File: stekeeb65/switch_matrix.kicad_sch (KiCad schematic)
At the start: 136 parts

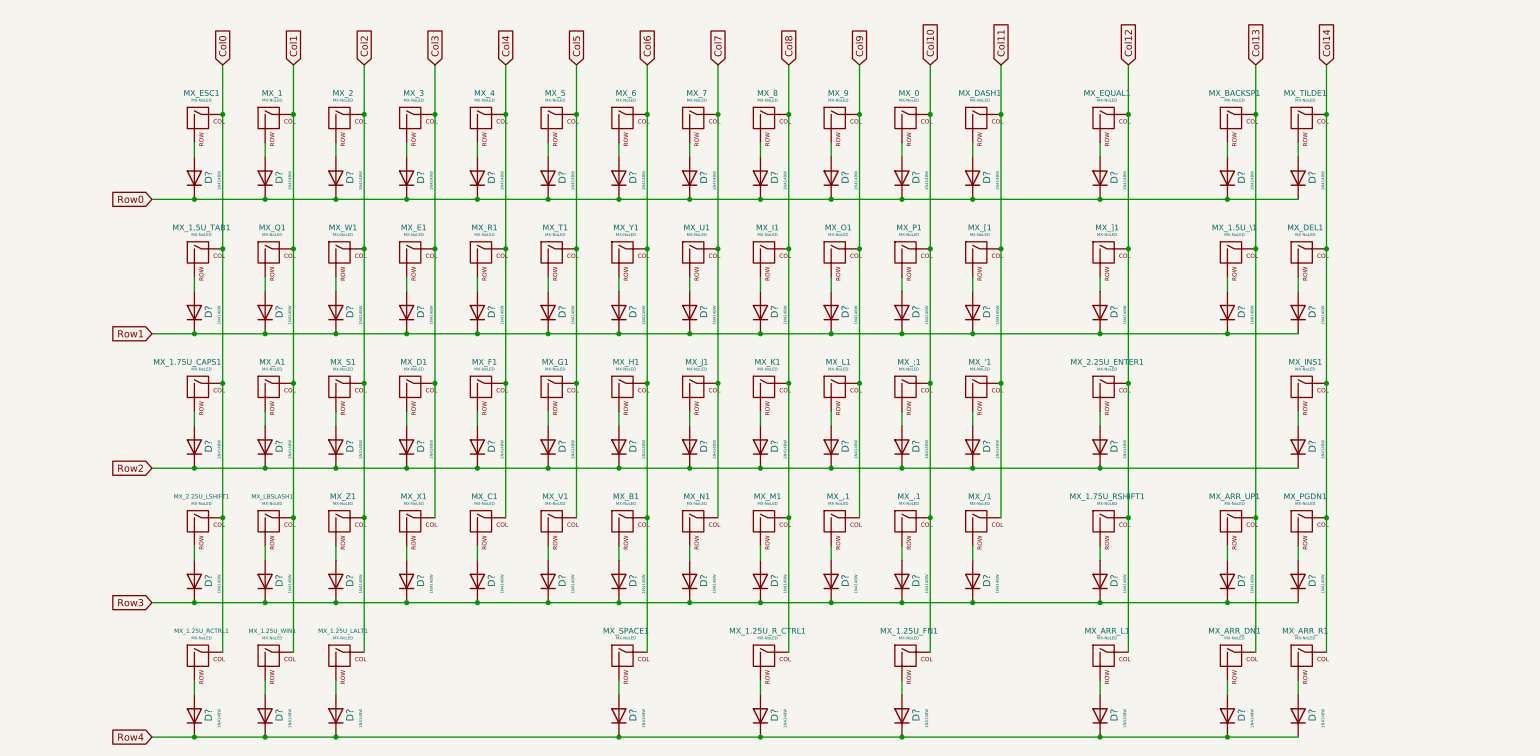
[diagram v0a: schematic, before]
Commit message: Adding keyboard footprints
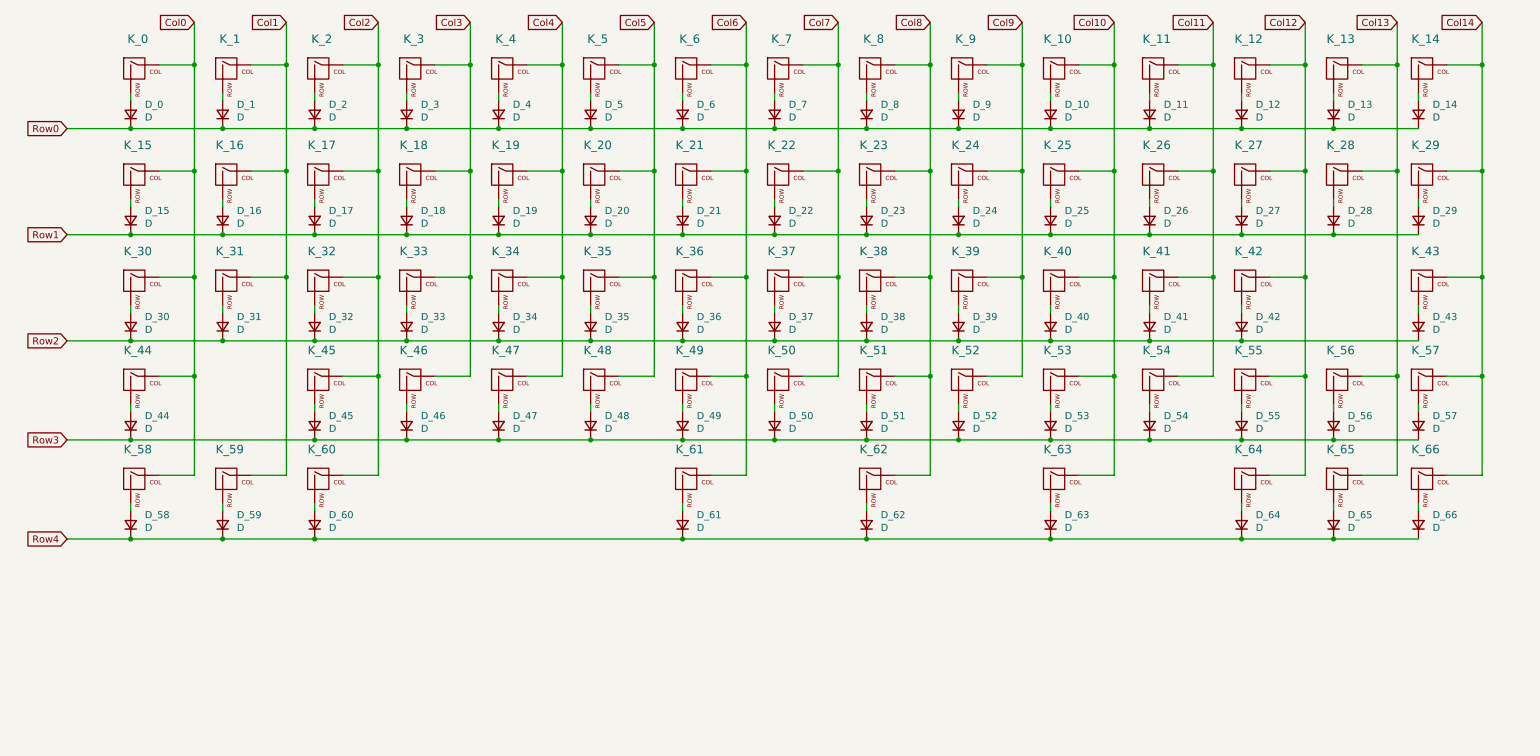
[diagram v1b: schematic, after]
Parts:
- removed D? (x68): 1N4148W, Diode_SMD:D_SOD-123, symbol Diode:1N4148W
- removed MX_'1, MX_,1, MX_.1, MX_/1, MX_0, MX_1, MX_1.25U_FN1, MX_1.25U_LALT1, MX_1.25U_RCTRL1, MX_1.25U_R_CTRL1, MX_1.25U_WIN1, MX_1.5U_TAB1, MX_1.5U_\1, MX_1.75U_CAPS1, MX_1.75U_RSHIFT1, MX_2, MX_2.25U_ENTER1, MX_2.25U_LSHIFT1, MX_3, MX_4, MX_5, MX_6, MX_7, MX_8, MX_9, MX_;1, MX_A1, MX_ARR_DN1, MX_ARR_L1, MX_ARR_R1, MX_ARR_UP1, MX_B1, MX_BACKSP1, MX_C1, MX_D1, MX_DASH1, MX_DEL1, MX_E1, MX_EQUAL1, MX_ESC1, MX_F1, MX_G1, MX_H1, MX_I1, MX_INS1, MX_J1, MX_K1, MX_L1, MX_LBSLASH1, MX_M1, MX_N1, MX_O1, MX_P1, MX_PGDN1, MX_Q1, MX_R1, MX_S1, MX_SPACE1, MX_T1, MX_TILDE1, MX_U1, MX_V1, MX_W1, MX_X1, MX_Y1, MX_Z1, MX_[1, MX_]1: MX-NoLED, symbol MX_Alps_Hybrid:MX-NoLED
- added D_0, D_1, D_10, D_11, D_12, D_13, D_14, D_15, D_16, D_17, D_18, D_19, D_2, D_20, D_21, D_22, D_23, D_24, D_25, D_26, D_27, D_28, D_29, D_3, D_30, D_31, D_32, D_33, D_34, D_35, D_36, D_37, D_38, D_39, D_4, D_40, D_41, D_42, D_43, D_44, D_45, D_46, D_47, D_48, D_49, D_5, D_50, D_51, D_52, D_53, D_54, D_55, D_56, D_57, D_58, D_59, D_6, D_60, D_61, D_62, D_63, D_64, D_65, D_66, D_7, D_8, D_9: D, Diode_SMD:D_SOD-123, symbol Device:D_Small
- added K_0, K_1, K_10, K_11, K_12, K_14, K_16, K_17, K_18, K_19, K_2, K_20, K_21, K_22, K_23, K_24, K_25, K_26, K_27, K_29, K_3, K_31, K_32, K_33, K_34, K_35, K_36, K_37, K_38, K_39, K_4, K_40, K_41, K_43, K_45, K_46, K_47, K_48, K_49, K_5, K_50, K_51, K_52, K_53, K_54, K_56, K_57, K_6, K_64, K_65, K_66, K_7, K_8, K_9: KEYSW, MX_Alps_Hybrid:MX-1U-NoLED, symbol MX_Alps_Hybrid:MX-NoLED
- added K_13: KEYSW, MX_Alps_Hybrid:MX-2U-NoLED, symbol MX_Alps_Hybrid:MX-NoLED
- added K_15, K_28: KEYSW, MX_Alps_Hybrid:MX-1.5U-NoLED, symbol MX_Alps_Hybrid:MX-NoLED
- added K_30, K_55: KEYSW, MX_Alps_Hybrid:MX-1.75U-NoLED, symbol MX_Alps_Hybrid:MX-NoLED
- added K_42, K_44: KEYSW, MX_Alps_Hybrid:MX-2.25U-NoLED, symbol MX_Alps_Hybrid:MX-NoLED
- added K_58, K_59, K_60, K_62, K_63: KEYSW, MX_Alps_Hybrid:MX-1.25U-NoLED, symbol MX_Alps_Hybrid:MX-NoLED
- added K_61: KEYSW, MX_Alps_Hybrid:MX-6.25U-NoLED, symbol MX_Alps_Hybrid:MX-NoLED
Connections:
- net Col0: now also K_0.1 (COL), K_15.1 (COL), K_30.1 (COL), K_44.1 (COL), K_58.1 (COL)
- net Col1: now also K_1.1 (COL), K_16.1 (COL), K_31.1 (COL), K_59.1 (COL)
- net Col10: now also K_10.1 (COL), K_25.1 (COL), K_40.1 (COL), K_53.1 (COL), K_63.1 (COL)
- net Col11: now also K_11.1 (COL), K_26.1 (COL), K_41.1 (COL), K_54.1 (COL)
- net Col12: now also K_12.1 (COL), K_27.1 (COL), K_42.1 (COL), K_55.1 (COL), K_64.1 (COL)
- net Col13: now also K_13.1 (COL), K_28.1 (COL), K_56.1 (COL), K_65.1 (COL)
- net Col14: now also K_14.1 (COL), K_29.1 (COL), K_43.1 (COL), K_57.1 (COL), K_66.1 (COL)
- net Col2: now also K_17.1 (COL), K_2.1 (COL), K_32.1 (COL), K_45.1 (COL), K_60.1 (COL)
- net Col3: now also K_18.1 (COL), K_3.1 (COL), K_33.1 (COL), K_46.1 (COL)
- net Col4: now also K_19.1 (COL), K_34.1 (COL), K_4.1 (COL), K_47.1 (COL)
- net Col5: now also K_20.1 (COL), K_35.1 (COL), K_48.1 (COL), K_5.1 (COL)
- net Col6: now also K_21.1 (COL), K_36.1 (COL), K_49.1 (COL), K_6.1 (COL), K_61.1 (COL)
- net Col7: now also K_22.1 (COL), K_37.1 (COL), K_50.1 (COL), K_7.1 (COL)
- net Col8: now also K_23.1 (COL), K_38.1 (COL), K_51.1 (COL), K_62.1 (COL), K_8.1 (COL)
- net Col9: now also K_24.1 (COL), K_39.1 (COL), K_52.1 (COL), K_9.1 (COL)
- net Row0: now also D_0.1 (K), D_1.1 (K), D_10.1 (K), D_11.1 (K), D_12.1 (K), D_13.1 (K), D_14.1 (K), D_2.1 (K), D_3.1 (K), D_4.1 (K), D_5.1 (K), D_6.1 (K), D_7.1 (K), D_8.1 (K), D_9.1 (K)
- net Row1: now also D_15.1 (K), D_16.1 (K), D_17.1 (K), D_18.1 (K), D_19.1 (K), D_20.1 (K), D_21.1 (K), D_22.1 (K), D_23.1 (K), D_24.1 (K), D_25.1 (K), D_26.1 (K), D_27.1 (K), D_28.1 (K), D_29.1 (K)
- net Row2: now also D_30.1 (K), D_31.1 (K), D_32.1 (K), D_33.1 (K), D_34.1 (K), D_35.1 (K), D_36.1 (K), D_37.1 (K), D_38.1 (K), D_39.1 (K), D_40.1 (K), D_41.1 (K), D_42.1 (K), D_43.1 (K)
- net Row3: now also D_44.1 (K), D_45.1 (K), D_46.1 (K), D_47.1 (K), D_48.1 (K), D_49.1 (K), D_50.1 (K), D_51.1 (K), D_52.1 (K), D_53.1 (K), D_54.1 (K), D_55.1 (K), D_56.1 (K), D_57.1 (K)
- net Row4: now also D_58.1 (K), D_59.1 (K), D_60.1 (K), D_61.1 (K), D_62.1 (K), D_63.1 (K), D_64.1 (K), D_65.1 (K), D_66.1 (K)
- new net: D_28.2 (A), K_28.2 (ROW)
- new net: D_19.2 (A), K_19.2 (ROW)
- new net: D_5.2 (A), K_5.2 (ROW)
- new net: D_26.2 (A), K_26.2 (ROW)
- new net: D_2.2 (A), K_2.2 (ROW)
- new net: D_47.2 (A), K_47.2 (ROW)
- new net: D_1.2 (A), K_1.2 (ROW)
- new net: D_27.2 (A), K_27.2 (ROW)
- new net: D_22.2 (A), K_22.2 (ROW)
- new net: D_10.2 (A), K_10.2 (ROW)
- new net: D_61.2 (A), K_61.2 (ROW)
- new net: D_21.2 (A), K_21.2 (ROW)
- new net: D_0.2 (A), K_0.2 (ROW)
- new net: D_23.2 (A), K_23.2 (ROW)
- new net: D_24.2 (A), K_24.2 (ROW)
- new net: D_30.2 (A), K_30.2 (ROW)
- new net: D_66.2 (A), K_66.2 (ROW)
- new net: D_16.2 (A), K_16.2 (ROW)
- new net: D_64.2 (A), K_64.2 (ROW)
- new net: D_6.2 (A), K_6.2 (ROW)
- new net: D_15.2 (A), K_15.2 (ROW)
- new net: D_65.2 (A), K_65.2 (ROW)
- new net: D_33.2 (A), K_33.2 (ROW)
- new net: D_37.2 (A), K_37.2 (ROW)
- new net: D_46.2 (A), K_46.2 (ROW)
- new net: D_18.2 (A), K_18.2 (ROW)
- new net: D_11.2 (A), K_11.2 (ROW)
- new net: D_56.2 (A), K_56.2 (ROW)
- new net: D_12.2 (A), K_12.2 (ROW)
- new net: D_31.2 (A), K_31.2 (ROW)
- new net: D_32.2 (A), K_32.2 (ROW)
- new net: D_8.2 (A), K_8.2 (ROW)
- new net: D_54.2 (A), K_54.2 (ROW)
- new net: D_40.2 (A), K_40.2 (ROW)
- new net: D_9.2 (A), K_9.2 (ROW)
- new net: D_13.2 (A), K_13.2 (ROW)
- new net: D_58.2 (A), K_58.2 (ROW)
- new net: D_38.2 (A), K_38.2 (ROW)
- new net: D_3.2 (A), K_3.2 (ROW)
- new net: D_36.2 (A), K_36.2 (ROW)
- new net: D_50.2 (A), K_50.2 (ROW)
- new net: D_7.2 (A), K_7.2 (ROW)
- new net: D_29.2 (A), K_29.2 (ROW)
- new net: D_4.2 (A), K_4.2 (ROW)
- new net: D_49.2 (A), K_49.2 (ROW)
- new net: D_35.2 (A), K_35.2 (ROW)
- new net: D_48.2 (A), K_48.2 (ROW)
- new net: D_53.2 (A), K_53.2 (ROW)
- new net: D_25.2 (A), K_25.2 (ROW)
- new net: D_52.2 (A), K_52.2 (ROW)
- new net: D_39.2 (A), K_39.2 (ROW)
- new net: D_44.2 (A), K_44.2 (ROW)
- new net: D_34.2 (A), K_34.2 (ROW)
- new net: D_41.2 (A), K_41.2 (ROW)
- new net: D_45.2 (A), K_45.2 (ROW)
- new net: D_20.2 (A), K_20.2 (ROW)
- new net: D_43.2 (A), K_43.2 (ROW)
- new net: D_42.2 (A), K_42.2 (ROW)
- new net: D_14.2 (A), K_14.2 (ROW)
- new net: D_63.2 (A), K_63.2 (ROW)
- new net: D_59.2 (A), K_59.2 (ROW)
- new net: D_57.2 (A), K_57.2 (ROW)
- new net: D_17.2 (A), K_17.2 (ROW)
- new net: D_55.2 (A), K_55.2 (ROW)
- new net: D_51.2 (A), K_51.2 (ROW)
- new net: D_62.2 (A), K_62.2 (ROW)
- new net: D_60.2 (A), K_60.2 (ROW)

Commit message: Committing before changes to PCB
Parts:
- K_0, K_1, K_10, K_11, K_12, K_14, K_16, K_17, K_18, K_19, K_2, K_20, K_21, K_22, K_23, K_24, K_25, K_26, K_27, K_29, K_3, K_31, K_32, K_33, K_34, K_35, K_36, K_37, K_38, K_39, K_4, K_40, K_41, K_43, K_45, K_46, K_47, K_48, K_49, K_5, K_50, K_51, K_52, K_53, K_54, K_56, K_57, K_6, K_64, K_65, K_66, K_7, K_8, K_9: footprint MX_Alps_Hybrid:MX-1U-NoLED -> MX_Hotswap:MX-Hotswap-1U
- K_13: footprint MX_Alps_Hybrid:MX-2U-NoLED -> MX_Hotswap:MX-Hotswap-2U
- K_15, K_28: footprint MX_Alps_Hybrid:MX-1.5U-NoLED -> MX_Hotswap:MX-Hotswap-1.5U
- K_30, K_55: footprint MX_Alps_Hybrid:MX-1.75U-NoLED -> MX_Hotswap:MX-Hotswap-1.75U
- K_42, K_44: footprint MX_Alps_Hybrid:MX-2.25U-NoLED -> MX_Hotswap:MX-Hotswap-2.25U
- K_58, K_59, K_60, K_62, K_63: footprint MX_Alps_Hybrid:MX-1.25U-NoLED -> MX_Hotswap:MX-Hotswap-1.25U
- K_61: footprint MX_Alps_Hybrid:MX-6.25U-NoLED -> MX_Hotswap:MX-Hotswap-6.25U-ReversedStabilizers

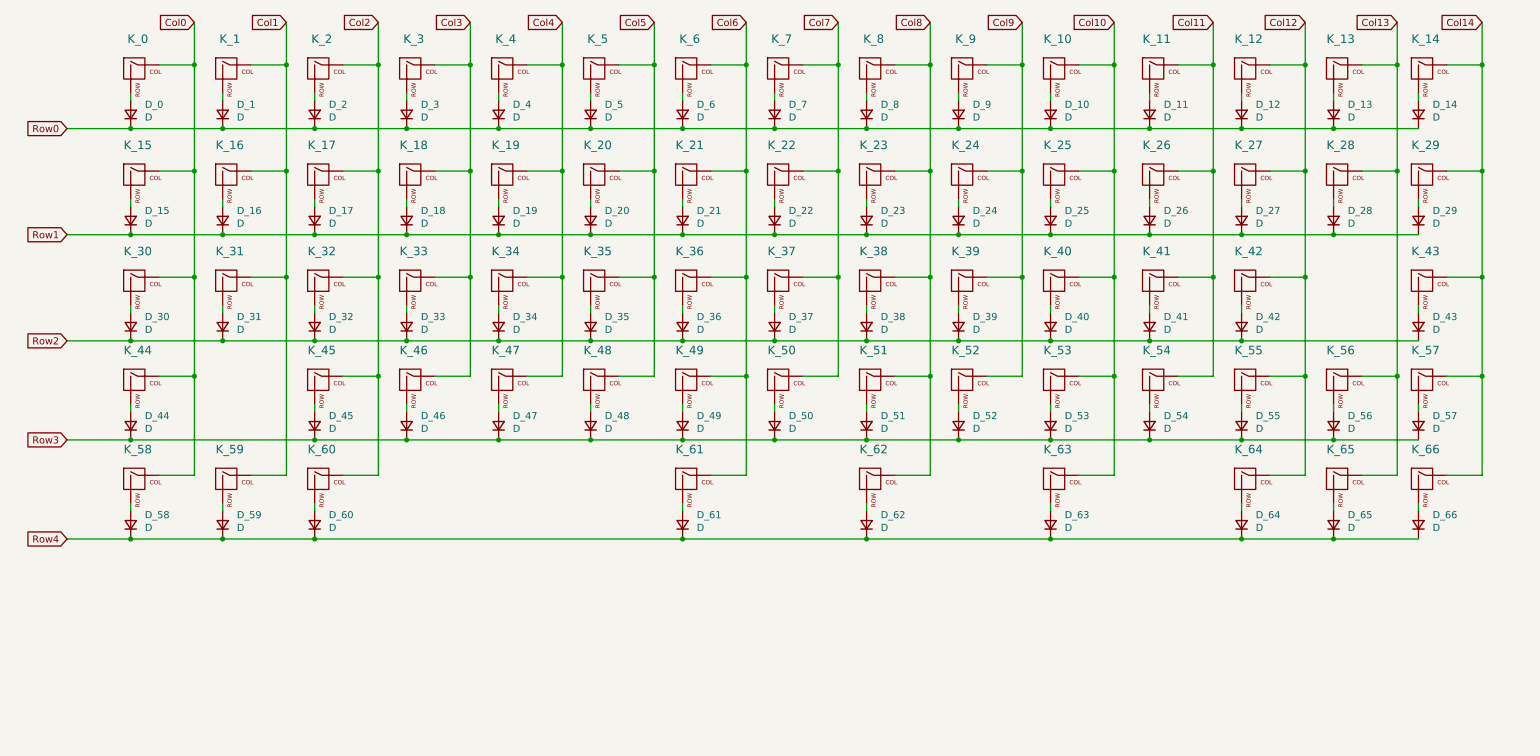
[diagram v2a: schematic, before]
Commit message: Adding layout for diodes, LEDs, edge cuts
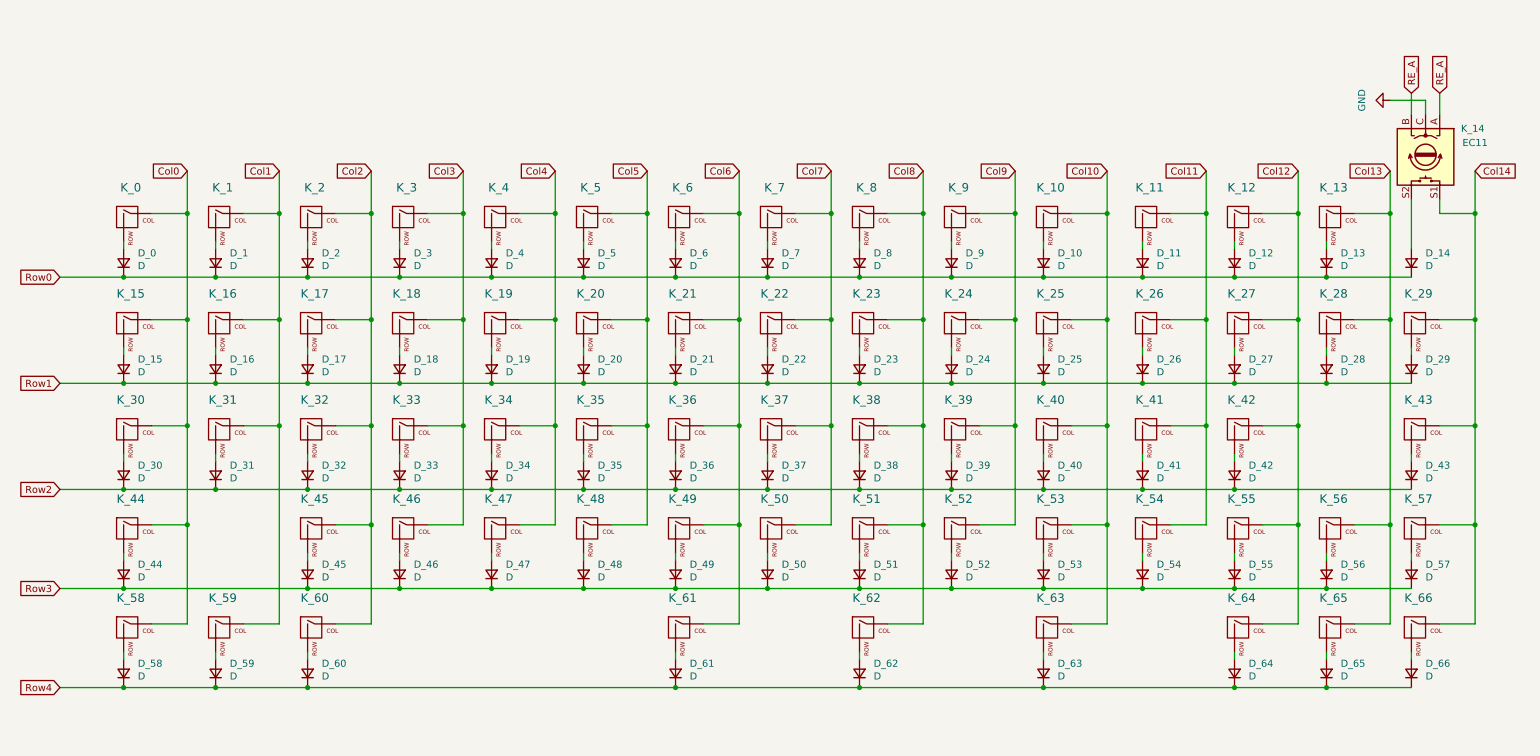
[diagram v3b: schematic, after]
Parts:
- removed K_14: KEYSW, MX_Hotswap:MX-Hotswap-1U, symbol MX_Alps_Hybrid:MX-NoLED
- added K_14: EC11, mini-general-tweaks:RotaryEncoder_Alps_EC11E-Switch-Vertical-EDIT, symbol Device:RotaryEncoder_Switch
- D_0, D_1, D_10, D_11, D_12, D_13, D_14, D_15, D_16, D_17, D_18, D_19, D_2, D_20, D_21, D_22, D_23, D_24, D_25, D_26, D_27, D_28, D_29, D_3, D_30, D_31, D_32, D_33, D_34, D_35, D_36, D_37, D_38, D_39, D_4, D_40, D_41, D_42, D_43, D_44, D_45, D_46, D_47, D_48, D_49, D_5, D_50, D_51, D_52, D_53, D_54, D_55, D_56, D_57, D_58, D_59, D_6, D_60, D_61, D_62, D_63, D_64, D_65, D_66, D_7, D_8, D_9: footprint Diode_SMD:D_SOD-123 -> random-keyboard-parts:D_SOD-123-Pretty
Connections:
- net Col14: now also K_14.S1
- net at D_14.2 (A): now also K_14.S2
- new net GND: K_14.C
- new net RE_A: K_14.A, K_14.B
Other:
- moved on the sheet: D_0, D_1, D_10, D_11, D_12, D_13, D_14, D_15, D_16, D_17, D_18, D_19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

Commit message: Redoing keyboard layout. Adding flex cuts to PCB
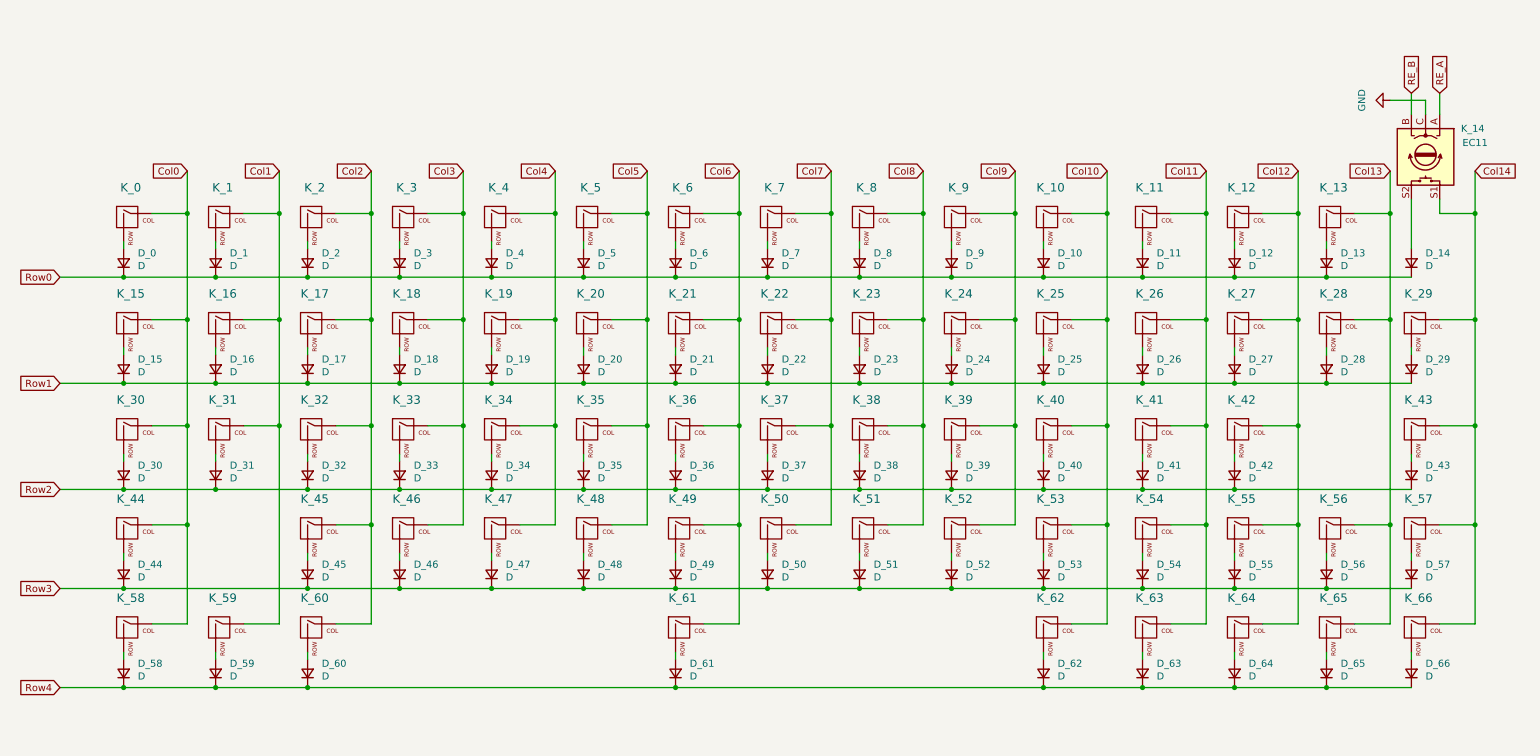
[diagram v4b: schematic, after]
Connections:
- net Col10: now also K_62.1 (COL); no longer K_63.1 (COL)
- net Col11: now also K_63.1 (COL)
- net Col8: no longer K_62.1 (COL)
- net RE_A: no longer K_14.B
- new net RE_B: K_14.B
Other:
- moved on the sheet: D_62, D_63, K_62, K_63
